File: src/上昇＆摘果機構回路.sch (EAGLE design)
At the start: 69 parts, among them SW2 SS-12SDP2, T1 2SC3325-Y,LF, T2 2SC3325, U1 MCP2517FD, X1 32.768K12.5PI/MC306, X2 RH100-24.000-18-1020-EXT-TR, X3 XRCGB40M000F4M01R0

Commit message: 1st fix
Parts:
- added C23: GRM21BC72A105KE01, GRM21BC72A105KE01(1uF):GRM21BC72A105KE01
- added C5: GRM31CR71H475KA12, GRM31CR71H475KA12:GRM31CR71H475KA12
- added FB1: BLM18KG121TN1D, BLM18KG121TN1D:BLM18KG121TN1D
- added JP3, JP4: (no value), pinhead:PINHD-1X2
- added JP5, JP6: (no value), pinhead:PINHD-1X4
- C24: value GRM31CR71H475KA12 -> GCM188L81H104KA57; device GRM31CR71H475KA12:GRM31CR71H475KA12 -> GCM188L81H104K57(0.1uF):GCM188L81H104KA57
- R12: value 10k -> 150
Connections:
- new net N$46: C23.P$1, C24.P$1, FB1.2, U$1.VDDA/VREF+
- net +3V3: now also FB1.1, U$1.VBAT
- net +5V: now also JP5.4
- net COM_LED: now also JP5.3
- net CS: now also JP6.1
- net MISO: now also JP6.2
- net MOSI: now also JP6.3
- net N$2: now also C5.1; no longer C24.1
- net SCK: now also JP6.4
- net SGND: now also C23.P$2, C24.P$2, C5.2, JP3.1, JP3.2, JP4.1, JP4.2, JP5.1; no longer C24.2
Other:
- note added: "DC電源ラインのノイズ対策インダクタンス"

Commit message: 3rd fix
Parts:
- removed C10, C9: GRM0335C1H6R0BA01D, GRM0335C1H6R0BA01D:GRM0335C1H6R0BA01D
- removed C6, C7, C8: GCM188L81H104KA57, GCM188L81H104K57(0.1uF):GCM188L81H104KA57
- removed JP2, JP3, JP4: (no value), pinhead:PINHD-1X2
- removed JP5, JP6: (no value), pinhead:PINHD-1X4
- removed R4: 120Ω, CR0603:CR0603
- removed R5: 0, CR0603:CR0603
- removed R6, R7: 150, CR0603:CR0603
- removed R8: 10k, CR0603:CR0603
- removed R9: 5.1k, CR0603:CR0603
- removed RJ45_3: MTJ-88ARX1-LH, MTJ-88ARX1-LH:MTJ-88ARX1-LH
- removed SW2: SS-12SDP2, SS-12SDP2:SS-12SDP2
- removed T2: 2SC3325, 2SC3325:2SC3325
- removed U$3: MCP2558FD, MCP2558FD:MCP2558FD
- removed U1: MCP2517FD, MCP2517FD:MCP2517FD
- removed X3: XRCGB40M000F4M01R0, XRCGB40M000F4M01R0:XRCGB40M000F4M01R0
- added LEFT, RIGHT: (no value), pinhead:PINHD-1X2
- added LEFT2, RIGHT2: (no value), pinhead:PINHD-1X4
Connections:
- removed net CAN_H: R4.RIGHT, RJ45_3.5, RJ45_3.6, U$3.CANH
- removed net CAN_L: RJ45_3.3, RJ45_3.4, SW2.C, U$3.CANL
- removed net N$12: U$3.TXD, U1.TXCAN
- removed net N$13: U$3.RXD, U1.RXCAN
- removed net N$14: R4.LEFT, SW2.R
- removed net N$15: C9.1, U1.OSC1, X3.1
- removed net N$16: C10.1, R5.RIGHT, X3.2
- removed net N$17: R5.LEFT, U1.OSC2
- removed net N$18: R6.LEFT, RJ45_3.LED2_A
- removed net N$20: JP2.2, U$3.S
- removed net N$21: R7.RIGHT, RJ45_3.LED1_A
- removed net N$24: RJ45_3.LED1_K, T2.C
- removed net N$29: R8.RIGHT, R9.LEFT, T2.B
- net +3V3: no longer C6.P$2, C8.P$1, U$3.VIO, U1.VDD
- net +5V: now also LEFT2.4; no longer C7.P$1, JP5.4, R6.RIGHT, R7.LEFT, RJ45_3.1, RJ45_3.7, U$3.VDD
- net COM_LED: now also LEFT2.3; no longer JP5.3, R9.RIGHT
- net CS: now also RIGHT2.1; no longer JP6.1, U1.NCS
- net MISO: now also RIGHT2.2; no longer JP6.2, U1.SDO
- net MOSI: now also RIGHT2.3; no longer JP6.3, U1.SDI
- net SCK: now also RIGHT2.4; no longer JP6.4, U1.SCK
- net SGND: now also LEFT.1, LEFT.2, LEFT2.1, RIGHT.1, RIGHT.2; no longer C10.2, C6.P$1, C7.P$2, C8.P$2, C9.2, JP2.1, JP3.1, JP3.2, JP4.1, JP4.2, JP5.1, R8.LEFT, RJ45_3.2, RJ45_3.8, RJ45_3.LED2_K, T2.E, U$3.VSS, U1.VSS
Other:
- note added: "CAN_BUS"
- note removed: "CAN BUS"
- note removed: "Default:closed"
- note removed: "RJ45(CH1)"
- note removed: "S=GND->normal mode S=VIN->silent mode"

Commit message: servo
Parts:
- added SERVO: 02-JST, con-jst-xh (1):02-JST
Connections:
- new net PWM_SERVO: SERVO.2, U$1.PB0
- net SGND: now also SERVO.1
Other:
- note added: "servo_PWMsupply_con"
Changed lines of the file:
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@@
 <part name="SUPPLY22" library="supply2" library_urn="urn:adsk.eagle:library:372" deviceset="GND" device=""/>
 <part name="SUPPLY23" library="supply2" library_urn="urn:adsk.eagle:library:372" deviceset="GND" device=""/>
+<part name="SERVO" library="con-jst-xh (1)" deviceset="02-JST" device=""/>
+<part name="SUPPLY24" library="supply2" library_urn="urn:adsk.eagle:library:372" deviceset="GND" device=""/>
 </parts>
 <sheets>
@@
 <wire x1="-185.42" y1="-81.28" x2="-185.42" y2="-33.02" width="0.1524" layer="97"/>
 <wire x1="-185.42" y1="-33.02" x2="-243.84" y2="-33.02" width="0.1524" layer="97"/>
+<wire x1="-157.48" y1="78.74" x2="-157.48" y2="106.68" width="0.1524" layer="97"/>
+<wire x1="-157.48" y1="106.68" x2="-93.98" y2="106.68" width="0.1524" layer="97"/>
+<wire x1="-93.98" y1="106.68" x2="-93.98" y2="78.74" width="0.1524" layer="97"/>
+<wire x1="-93.98" y1="78.74" x2="-157.48" y2="78.74" width="0.1524" layer="97"/>
+<text x="-154.94" y="101.6" size="3.81" layer="97">servo_PWMsupply_con</text>
 </plain>
 <instances>
@@
 <instance part="SUPPLY22" gate="GND" x="-236.22" y="-73.66" smashed="yes"/>
 <instance part="SUPPLY23" gate="GND" x="-195.58" y="-73.66" smashed="yes"/>
+<instance part="SERVO" gate="G$1" x="-137.16" y="91.44" smashed="yes">
+<attribute name="VALUE" x="-138.43" y="83.82" size="1.778" layer="96"/>
+<attribute name="NAME" x="-138.43" y="94.742" size="1.778" layer="95"/>
+</instance>
+<instance part="SUPPLY24" gate="GND" x="-124.46" y="83.82" smashed="yes"/>
 </instances>
 <busses>
@@
 <label x="-198.12" y="-76.2" size="1.778" layer="95"/>
 </segment>
+<segment>
+<pinref part="SERVO" gate="G$1" pin="1"/>
+<wire x1="-129.54" y1="88.9" x2="-124.46" y2="88.9" width="0.1524" layer="91"/>
+<wire x1="-124.46" y1="88.9" x2="-124.46" y2="86.36" width="0.1524" layer="91"/>
+<pinref part="SUPPLY24" gate="GND" pin="GND"/>
+<label x="-127" y="81.28" size="1.778" layer="95"/>
+</segment>
 </net>
 <net name="DIR4" class="0">
@@
 </segment>
 </net>
+<net name="PWM_SERVO" class="0">
+<segment>
+<pinref part="SERVO" gate="G$1" pin="2"/>
+<wire x1="-129.54" y1="91.44" x2="-114.3" y2="91.44" width="0.1524" layer="91"/>
+<label x="-129.54" y="91.44" size="1.778" layer="95"/>
+</segment>
+<segment>
+<pinref part="U$1" gate="G$1" pin="PB0"/>
+<wire x1="5.08" y1="48.26" x2="5.08" y2="35.56" width="0.1524" layer="91"/>
+<label x="5.08" y="35.56" size="1.778" layer="95" rot="R90"/>
+</segment>
+</net>

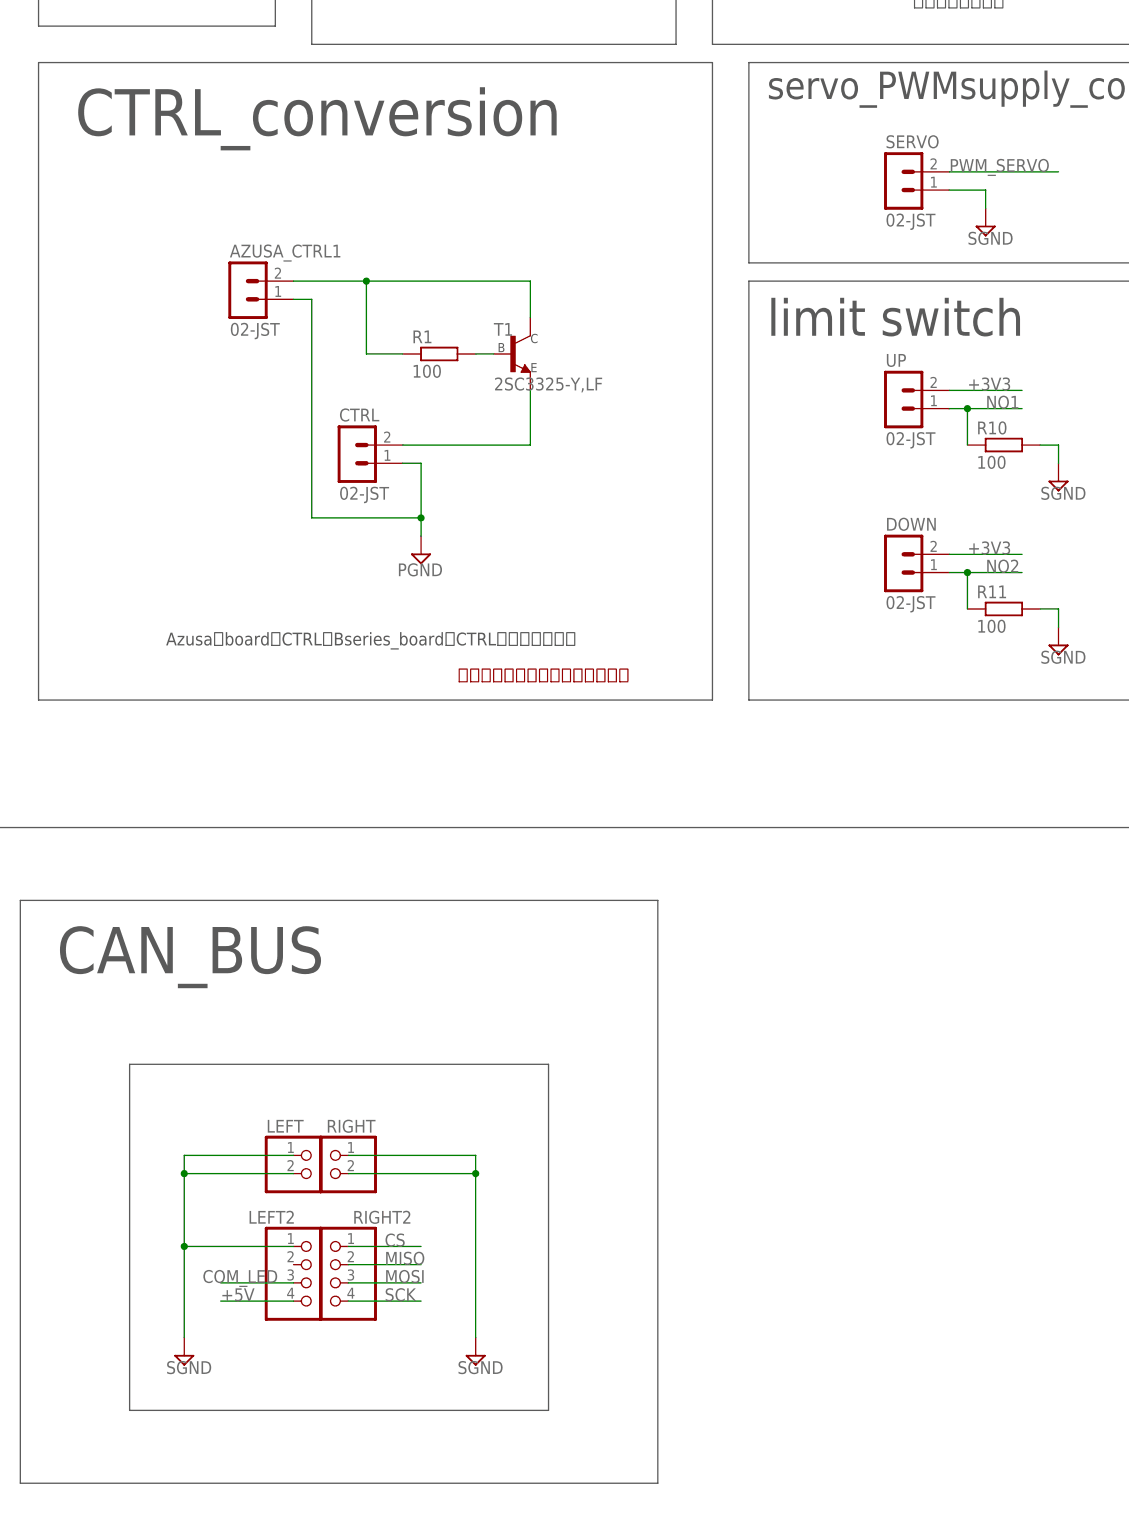
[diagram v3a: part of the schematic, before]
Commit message: add serbo pin
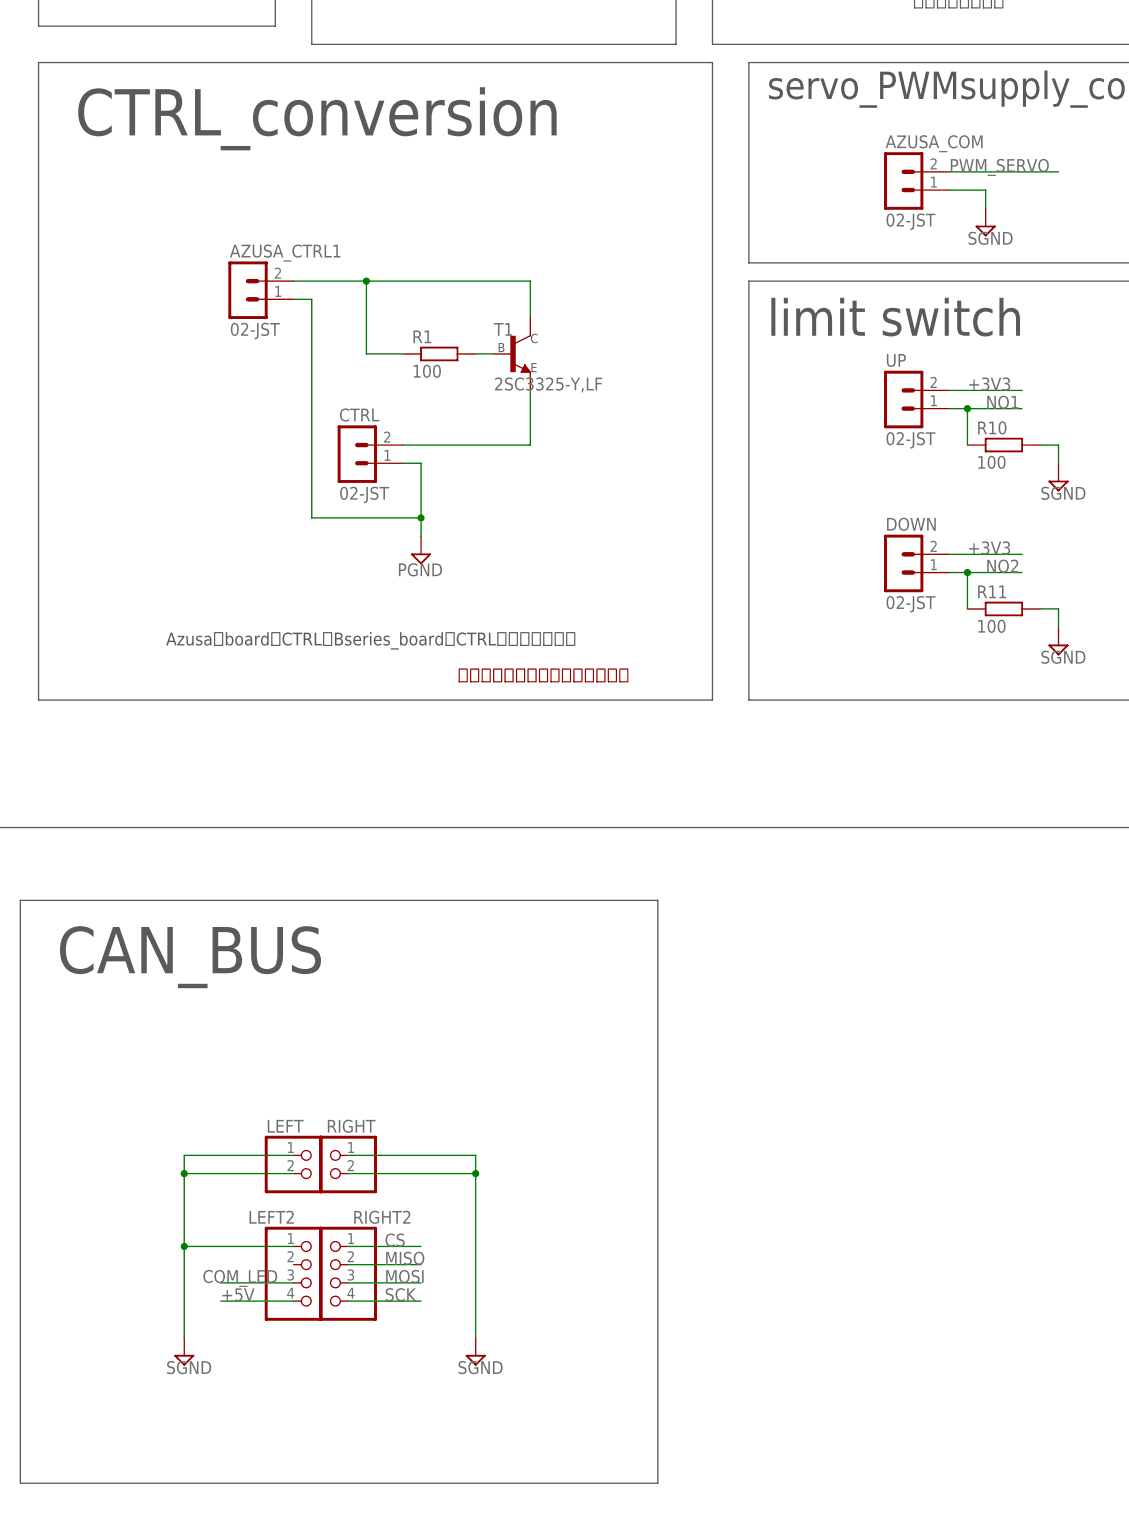
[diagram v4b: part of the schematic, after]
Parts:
- renumbered SERVO to AZUSA_COM
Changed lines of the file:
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@@
 <part name="SUPPLY22" library="supply2" library_urn="urn:adsk.eagle:library:372" deviceset="GND" device=""/>
 <part name="SUPPLY23" library="supply2" library_urn="urn:adsk.eagle:library:372" deviceset="GND" device=""/>
-<part name="SERVO" library="con-jst-xh (1)" deviceset="02-JST" device=""/>
+<part name="AZUSA_COM" library="con-jst-xh (1)" deviceset="02-JST" device=""/>
 <part name="SUPPLY24" library="supply2" library_urn="urn:adsk.eagle:library:372" deviceset="GND" device=""/>
 </parts>
@@
 <text x="26.416" y="40.894" size="1.778" layer="95">C5</text>
 <text x="-88.9" y="48.26" size="1.778" layer="97">DC電源ラインのノイズ対策インダクタンス</text>
-<wire x1="-243.84" y1="-33.02" x2="-243.84" y2="-81.28" width="0.1524" layer="97"/>
-<wire x1="-243.84" y1="-81.28" x2="-185.42" y2="-81.28" width="0.1524" layer="97"/>
-<wire x1="-185.42" y1="-81.28" x2="-185.42" y2="-33.02" width="0.1524" layer="97"/>
-<wire x1="-185.42" y1="-33.02" x2="-243.84" y2="-33.02" width="0.1524" layer="97"/>
 <wire x1="-157.48" y1="78.74" x2="-157.48" y2="106.68" width="0.1524" layer="97"/>
 <wire x1="-157.48" y1="106.68" x2="-93.98" y2="106.68" width="0.1524" layer="97"/>
@@
 <instance part="SUPPLY22" gate="GND" x="-236.22" y="-73.66" smashed="yes"/>
 <instance part="SUPPLY23" gate="GND" x="-195.58" y="-73.66" smashed="yes"/>
-<instance part="SERVO" gate="G$1" x="-137.16" y="91.44" smashed="yes">
+<instance part="AZUSA_COM" gate="G$1" x="-137.16" y="91.44" smashed="yes">
 <attribute name="VALUE" x="-138.43" y="83.82" size="1.778" layer="96"/>
 <attribute name="NAME" x="-138.43" y="94.742" size="1.778" layer="95"/>
@@
 </segment>
 <segment>
-<pinref part="SERVO" gate="G$1" pin="1"/>
+<pinref part="AZUSA_COM" gate="G$1" pin="1"/>
 <wire x1="-129.54" y1="88.9" x2="-124.46" y2="88.9" width="0.1524" layer="91"/>
 <wire x1="-124.46" y1="88.9" x2="-124.46" y2="86.36" width="0.1524" layer="91"/>
@@
 <net name="PWM_SERVO" class="0">
 <segment>
-<pinref part="SERVO" gate="G$1" pin="2"/>
+<pinref part="AZUSA_COM" gate="G$1" pin="2"/>
 <wire x1="-129.54" y1="91.44" x2="-114.3" y2="91.44" width="0.1524" layer="91"/>
 <label x="-129.54" y="91.44" size="1.778" layer="95"/>
